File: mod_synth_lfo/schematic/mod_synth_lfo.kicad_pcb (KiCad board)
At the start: 2 copper layers, 80.6 x 109.2 mm, 78 parts, among them J1 CV, J2 Conn_02x08_Odd_Even, J3 SIN, J4 COS, J5 TRI, J6 SQR, J7 RAMP UP, J8 RAMP DOWN, Q1 BC550, Q2 BC550, Q3 BC550, Q4 BC550, Q5 BC550, U1 TL072, U2 TL072, U3 TL072, U4 TL074

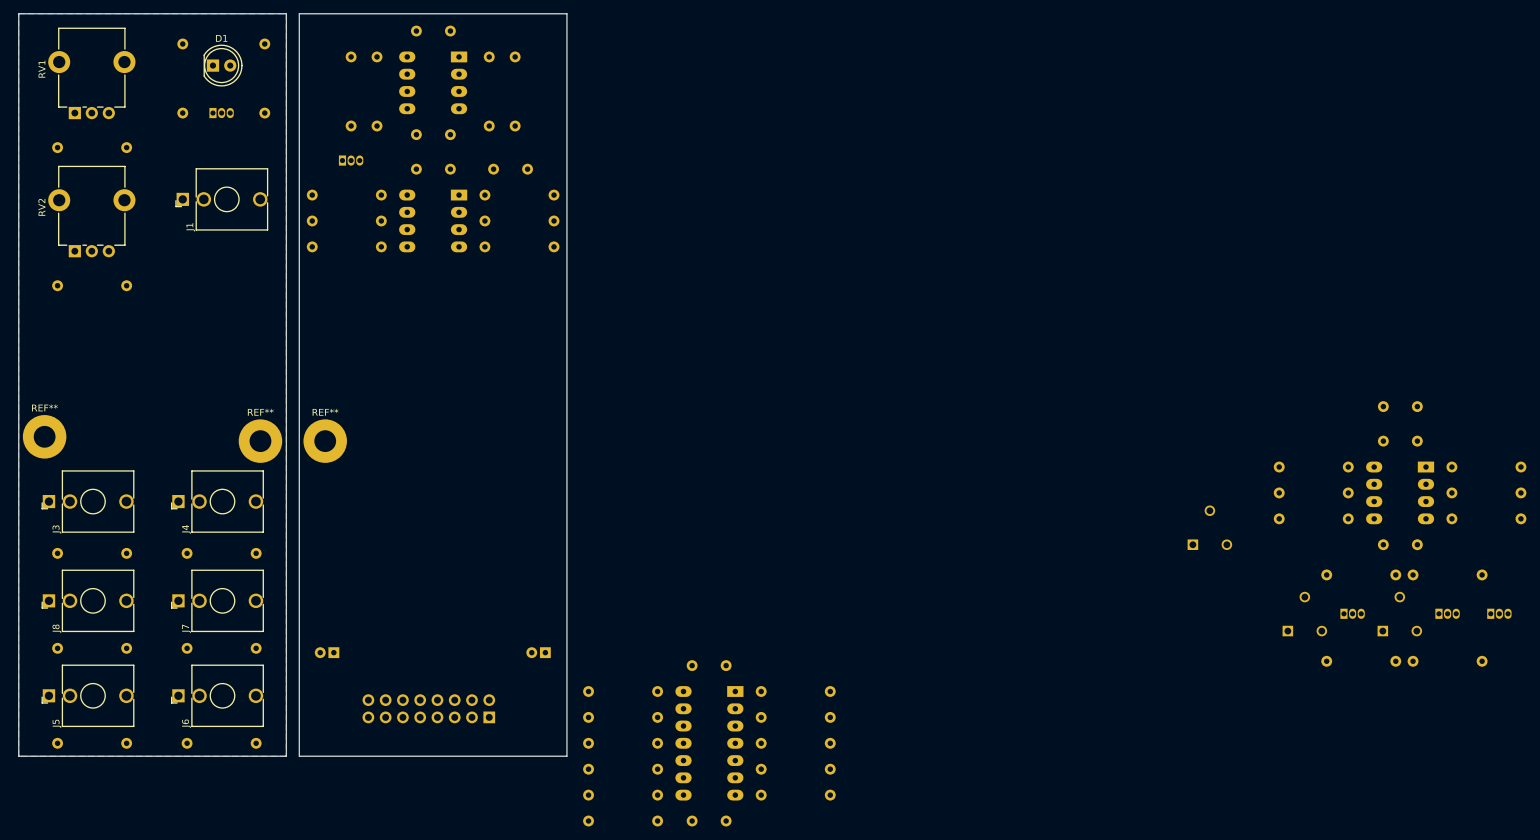
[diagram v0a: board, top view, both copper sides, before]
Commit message: Remove ramp and sin outputs
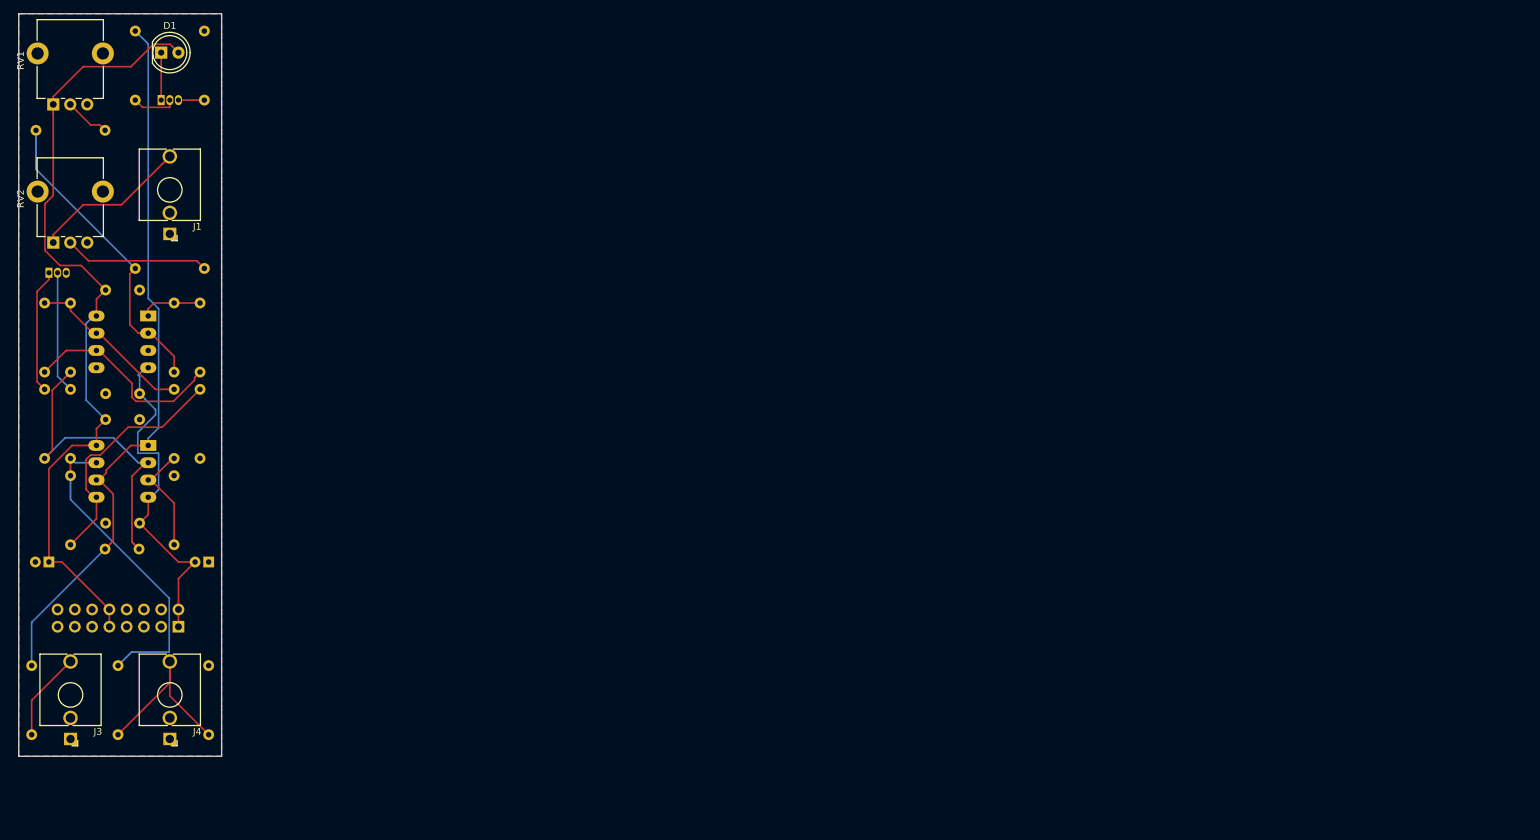
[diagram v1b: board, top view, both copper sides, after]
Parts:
- removed C10, C11, C8, C9: 100nf, Capacitor_THT:C_Disc_D9.0mm_W2.5mm_P5.00mm
- removed the J3 at (32.4, 87.0)
- removed the J4 at (51.4, 87.0)
- removed J7: RAMP UP, Connector_Audio:Jack_3.5mm_QingPu_WQP-PJ398SM_Vertical_CircularHoles
- removed J8: RAMP DOWN, Connector_Audio:Jack_3.5mm_QingPu_WQP-PJ398SM_Vertical_CircularHoles
- removed the Q2 at (236.9, 103.5)
- removed Q3, Q4: BC550, Package_TO_SOT_THT:TO-92_Inline
- removed the R12 at (213.4, 81.9)
- removed the R14 at (233.0, 97.8)
- removed the R15 at (233.0, 110.5)
- removed the R16 at (220.3, 110.5)
- removed the R17 at (230.5, 97.8)
- removed R18, R29, R33, R34, R35, R39: 10k, Resistor_THT:R_Axial_DIN0207_L6.3mm_D2.5mm_P10.16mm_Horizontal
- removed R19, R20, R21, R25: 100k, Resistor_THT:R_Axial_DIN0207_L6.3mm_D2.5mm_P10.16mm_Horizontal
- removed R22: 470, Resistor_THT:R_Axial_DIN0207_L6.3mm_D2.5mm_P10.16mm_Horizontal
- removed R24, R26: 33k, Resistor_THT:R_Axial_DIN0207_L6.3mm_D2.5mm_P10.16mm_Horizontal
- removed R27: 50k, Resistor_THT:R_Axial_DIN0207_L6.3mm_D2.5mm_P10.16mm_Horizontal
- removed R28: 20k, Resistor_THT:R_Axial_DIN0207_L6.3mm_D2.5mm_P10.16mm_Horizontal
- removed R32, R37, R40, R41: 1k, Resistor_THT:R_Axial_DIN0207_L6.3mm_D2.5mm_P10.16mm_Horizontal
- removed REF** (x3): MountingHole_3.2mm_M3_Pad, MountingHole:MountingHole_3.2mm_M3_Pad
- removed RV3: 100k, Potentiometer_THT:Potentiometer_Runtron_RM-065_Vertical
- removed RV4: 50k, Potentiometer_THT:Potentiometer_Runtron_RM-065_Vertical
- removed RV5: 20k, Potentiometer_THT:Potentiometer_Runtron_RM-065_Vertical
- removed U3: TL072, Package_DIP:DIP-8_W7.62mm_Socket_LongPads
- removed U4: TL074, Package_DIP:DIP-14_W7.62mm_Socket_LongPads
- moved C5 189.3 mm to (45.7, 55.9)
- moved C6 189.3 mm to (45.7, 71.1)
- moved C3 100.5 mm to (45.7, 74.9), turned to 180 degrees
- moved R12 87.8 mm to (35.6, 93.3), turned to 90 degrees
- moved C4 83.9 mm to (45.7, 90.2), turned to 180 degrees
- moved C7 79.9 mm to (40.6, 94.0)
- moved R8 68.1 mm to (31.8, 70.5), turned to 270 degrees
- moved R9 67.3 mm to (50.8, 83.2), turned to 270 degrees
- moved U1 59.5 mm to (47.0, 59.7)
- moved R3 58.8 mm to (50.8, 57.8)
- moved R4 58.8 mm to (54.6, 67.9)
- moved U2 58.7 mm to (47.0, 78.7)
- moved R5 57.8 mm to (31.8, 57.8)
- moved R6 57.8 mm to (35.6, 67.9)
- moved R14 57.3 mm to (55.9, 121.3), turned to 90 degrees
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- renumbered J5 to J3, J6 to J4, Q5 to Q2, R13 to R12, R23 to R13, R30 to R14, R36 to R15, R38 to R16, R42 to R17
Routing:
- net +12V: track 0.00 -> 119.1 mm
- net Net-(C7-Pad1): track 0.00 -> 106.1 mm
- net -12V: track 0.00 -> 51.2 mm
- net Net-(R10-Pad2): track 0.00 -> 46.9 mm
- net Net-(C7-Pad2): track 0.00 -> 46.7 mm
- net Net-(R1-Pad1): track 0.00 -> 45.7 mm
- net Net-(R11-Pad2): track 0.00 -> 36.0 mm
- net Net-(R4-Pad1): track 0.00 -> 30.5 mm
- net Net-(J4-PadT): track 0.00 -> 27.1 mm
- net Net-(R5-Pad1): track 0.00 -> 25.0 mm
- net Net-(J1-PadT): track 0.00 -> 23.1 mm
- net Net-(R2-Pad2): track 0.00 -> 21.3 mm
- net Net-(Q1-Pad1): track 0.00 -> 18.3 mm
- net Net-(Q1-Pad2): track 0.00 -> 17.9 mm
- net Net-(R7-Pad1): track 0.00 -> 16.1 mm
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- added copper zone on F.Cu, net GND
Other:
- board size 80.6 x 109.2 mm -> 29.8 x 109.2 mm

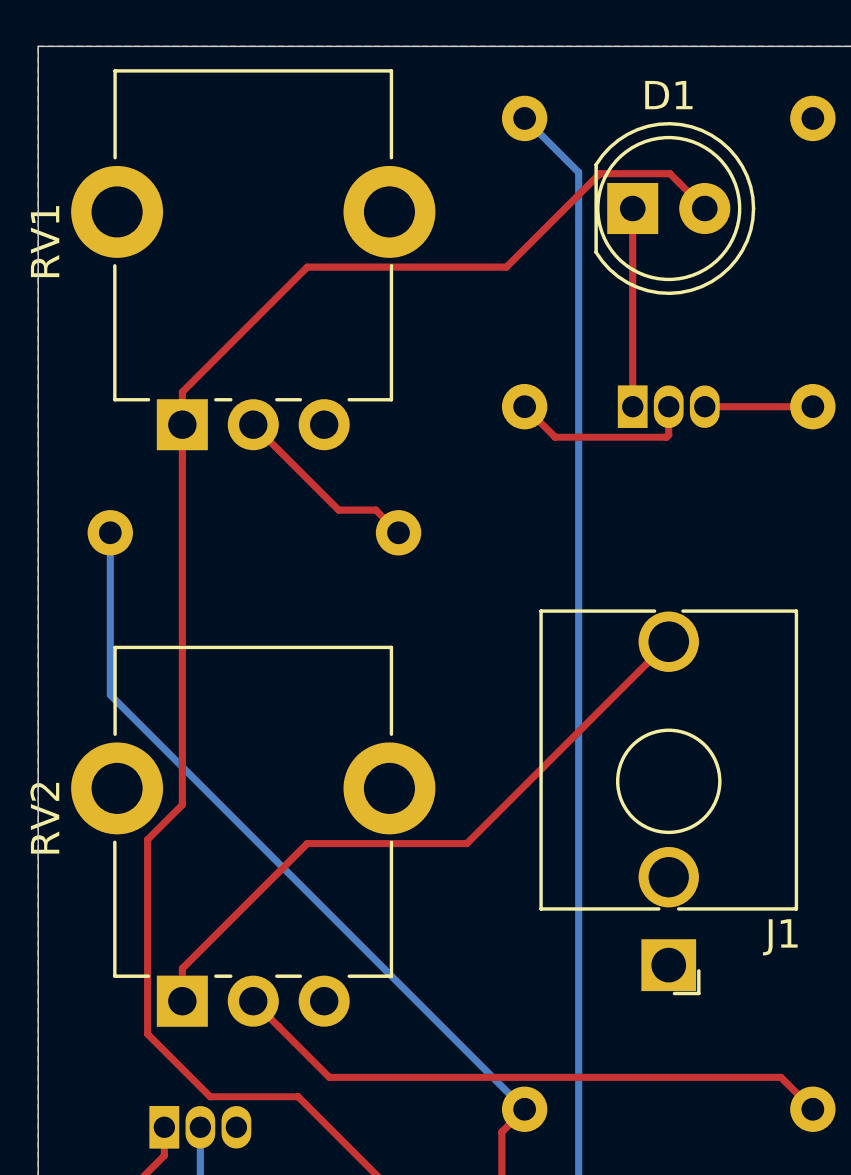
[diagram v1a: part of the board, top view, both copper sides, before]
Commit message: Reverse pots
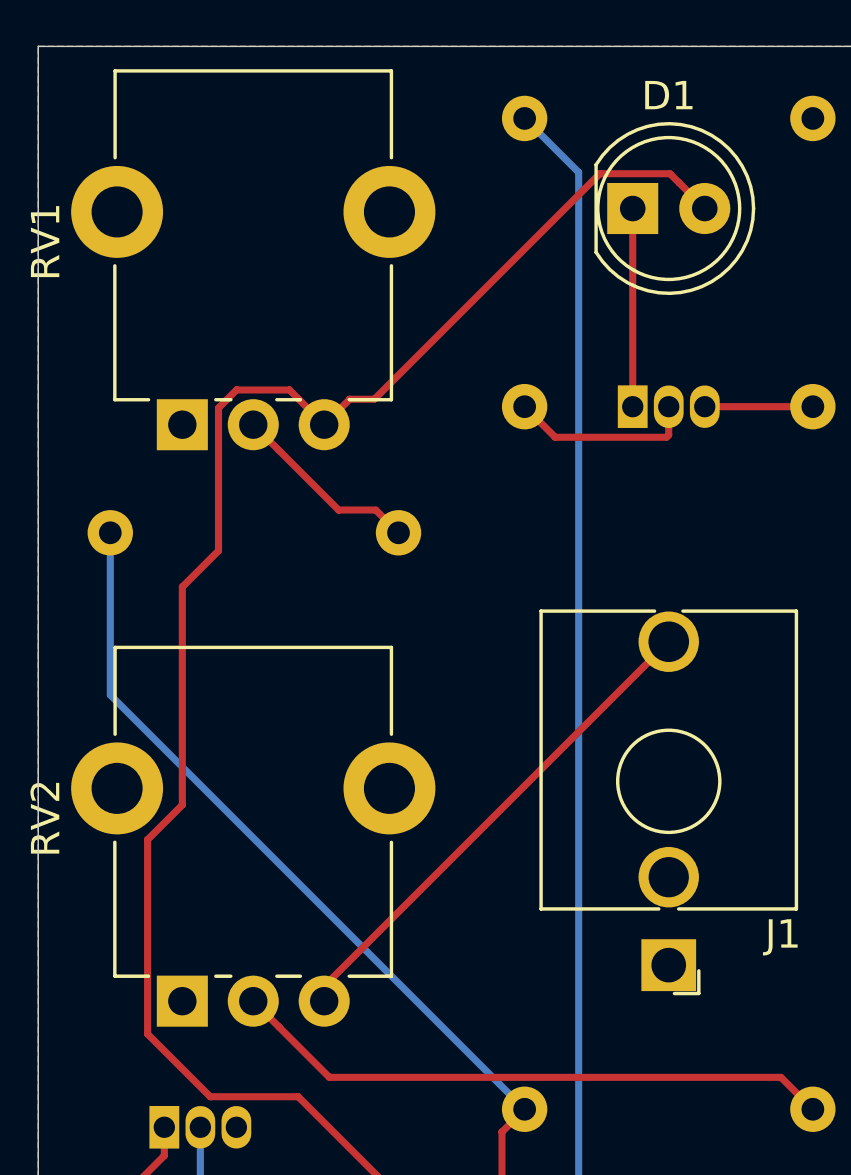
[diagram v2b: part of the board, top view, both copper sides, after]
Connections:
- RV1 pad 1: +12V -> GND
- RV1 pad 3: GND -> +12V
- RV2 pad 1: Net-(J1-PadT) -> GND
- RV2 pad 3: GND -> Net-(J1-PadT)
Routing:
- net Net-(J1-PadT): track 23.1 -> 17.7 mm
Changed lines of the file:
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@@
     (thickness 1.6)
     (drawings 4)
-    (tracks 170)
+    (tracks 171)
     (zones 0)
     (modules 35)
@@
     (pad "" thru_hole circle (at 7.5 7.3 180) (size 3.24 3.24) (drill 1.8) (layers *.Cu *.Mask))
     (pad 3 thru_hole circle (at 0 5 180) (size 1.8 1.8) (drill 1) (layers *.Cu *.Mask)
-      (net 1 GND))
+      (net 7 "Net-(J1-PadT)"))
     (pad 2 thru_hole circle (at 0 2.5 180) (size 1.8 1.8) (drill 1) (layers *.Cu *.Mask)
       (net 22 "Net-(R2-Pad2)"))
     (pad 1 thru_hole rect (at 0 0 180) (size 1.8 1.8) (drill 1) (layers *.Cu *.Mask)
-      (net 7 "Net-(J1-PadT)"))
+      (net 1 GND))
     (model ${KISYS3DMOD}/Potentiometer_THT.3dshapes/Potentiometer_Alpha_RD901F-40-00D_Single_Vertical.wrl
       (at (xyz 0 0 0))
@@
     (pad "" thru_hole circle (at 7.5 7.3 180) (size 3.24 3.24) (drill 1.8) (layers *.Cu *.Mask))
     (pad 3 thru_hole circle (at 0 5 180) (size 1.8 1.8) (drill 1) (layers *.Cu *.Mask)
-      (net 1 GND))
+      (net 2 +12V))
     (pad 2 thru_hole circle (at 0 2.5 180) (size 1.8 1.8) (drill 1) (layers *.Cu *.Mask)
       (net 20 "Net-(R1-Pad2)"))
     (pad 1 thru_hole rect (at 0 0 180) (size 1.8 1.8) (drill 1) (layers *.Cu *.Mask)
-      (net 2 +12V))
+      (net 1 GND))
     (model ${KISYS3DMOD}/Potentiometer_THT.3dshapes/Potentiometer_Alpha_RD901F-40-00D_Single_Vertical.wrl
       (at (xyz 0 0 0))
@@
   (gr_line (start 57.785 15.24) (end 57.785 124.46) (layer Edge.Cuts) (width 0.05))
   (gr_line (start 27.94 15.24) (end 57.785 15.24) (layer Edge.Cuts) (width 0.05))
-  (segment (start 50.535001 20.055001) (end 51.435 20.955) (width 0.25) (layer F.Cu) (net 2))
-  (segment (start 50.209999 19.729999) (end 50.535001 20.055001) (width 0.25) (layer F.Cu) (net 2))
-  (segment (start 47.734999 19.729999) (end 50.209999 19.729999) (width 0.25) (layer F.Cu) (net 2))
-  (segment (start 44.444997 23.020001) (end 47.734999 19.729999) (width 0.25) (layer F.Cu) (net 2))
-  (segment (start 37.424999 23.020001) (end 44.444997 23.020001) (width 0.25) (layer F.Cu) (net 2))
-  (segment (start 33.02 27.425) (end 37.424999 23.020001) (width 0.25) (layer F.Cu) (net 2))
-  (segment (start 33.02 28.575) (end 33.02 27.425) (width 0.25) (layer F.Cu) (net 2))
   (segment (start 41.275 105.41) (end 41.275 102.87) (width 0.25) (layer F.Cu) (net 2))
   (segment (start 34.29 95.885) (end 32.385 95.885) (width 0.25) (layer F.Cu) (net 2))
@@
   (segment (start 39.37 57.23) (end 40.72 55.88) (width 0.25) (layer F.Cu) (net 2))
   (segment (start 39.37 59.69) (end 39.37 57.23) (width 0.25) (layer F.Cu) (net 2))
-  (segment (start 33.02 29.725) (end 33.02 28.575) (width 0.25) (layer F.Cu) (net 2))
-  (segment (start 33.02 41.973602) (end 33.02 29.725) (width 0.25) (layer F.Cu) (net 2))
   (segment (start 31.794999 43.198603) (end 33.02 41.973602) (width 0.25) (layer F.Cu) (net 2))
   (segment (start 31.794999 50.055001) (end 31.794999 43.198603) (width 0.25) (layer F.Cu) (net 2))
@@
   (segment (start 37.84499 72.05499) (end 37.84499 60.81501) (width 0.25) (layer B.Cu) (net 2))
   (segment (start 40.72 74.93) (end 37.84499 72.05499) (width 0.25) (layer B.Cu) (net 2))
+  (segment (start 37.120001 27.675001) (end 38.02 28.575) (width 0.25) (layer F.Cu) (net 2))
+  (segment (start 36.794999 27.349999) (end 37.120001 27.675001) (width 0.25) (layer F.Cu) (net 2))
+  (segment (start 34.931999 27.349999) (end 36.794999 27.349999) (width 0.25) (layer F.Cu) (net 2))
+  (segment (start 34.294999 27.986999) (end 34.931999 27.349999) (width 0.25) (layer F.Cu) (net 2))
+  (segment (start 34.294999 33.015001) (end 34.294999 27.986999) (width 0.25) (layer F.Cu) (net 2))
+  (segment (start 33.02 34.29) (end 34.294999 33.015001) (width 0.25) (layer F.Cu) (net 2))
+  (segment (start 33.02 41.973602) (end 33.02 34.29) (width 0.25) (layer F.Cu) (net 2))
+  (segment (start 50.535001 20.055001) (end 51.435 20.955) (width 0.25) (layer F.Cu) (net 2))
+  (segment (start 50.209999 19.729999) (end 50.535001 20.055001) (width 0.25) (layer F.Cu) (net 2))
+  (segment (start 47.734999 19.729999) (end 50.209999 19.729999) (width 0.25) (layer F.Cu) (net 2))
+  (segment (start 39.789997 27.675001) (end 47.734999 19.729999) (width 0.25) (layer F.Cu) (net 2))
+  (segment (start 38.919999 27.675001) (end 39.789997 27.675001) (width 0.25) (layer F.Cu) (net 2))
+  (segment (start 38.02 28.575) (end 38.919999 27.675001) (width 0.25) (layer F.Cu) (net 2))
   (segment (start 51.435 98.33) (end 51.435 102.87) (width 0.25) (layer F.Cu) (net 3))
   (segment (start 53.88 95.885) (end 51.435 98.33) (width 0.25) (layer F.Cu) (net 3))
@@
   (segment (start 46.99 19.685) (end 46.99 57.104998) (width 0.25) (layer B.Cu) (net 5))
   (segment (start 48.895 20.955) (end 48.895 27.94) (width 0.25) (layer F.Cu) (net 6))
-  (segment (start 49.100001 37.289999) (end 50.165 36.225) (width 0.25) (layer F.Cu) (net 7))
-  (segment (start 43.049999 43.340001) (end 49.100001 37.289999) (width 0.25) (layer F.Cu) (net 7))
-  (segment (start 37.424999 43.340001) (end 43.049999 43.340001) (width 0.25) (layer F.Cu) (net 7))
-  (segment (start 33.02 47.745) (end 37.424999 43.340001) (width 0.25) (layer F.Cu) (net 7))
-  (segment (start 33.02 48.895) (end 33.02 47.745) (width 0.25) (layer F.Cu) (net 7))
+  (segment (start 38.02 48.37) (end 38.02 48.895) (width 0.25) (layer F.Cu) (net 7))
+  (segment (start 50.165 36.225) (end 38.02 48.37) (width 0.25) (layer F.Cu) (net 7))
   (segment (start 29.845 116.235) (end 35.56 110.52) (width 0.25) (layer F.Cu) (net 14))
   (segment (start 29.845 121.285) (end 29.845 116.235) (width 0.25) (layer F.Cu) (net 14))
